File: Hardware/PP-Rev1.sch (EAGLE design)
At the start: 169 parts, among them IC1 LT6004, IC2 TLC6C5912-Q1, Q1 MOSFET-PCHANNEL, Q10 2N7002PW, Q11 2N7002PW, Q12 2N7002PW, Q13 2N7002PW, Q14 2N7002PW, Q15 2N7002PW, Q2 MOSFET-PCHANNEL, Q3 MOSFET-PCHANNEL, Q4 MOSFET-PCHANNEL, Q5 MOSFET-PCHANNEL, Q6 MOSFET-PCHANNEL, Q7 MOSFET-PCHANNEL, Q8 MOSFET-PCHANNEL, Q9 CSD18532, X1 22-23-2031, X2 22-23-2031, X3 22-23-2031, X4 22-23-2031

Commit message: Added launchpad microcontroller library file and into schematic/board. Updated LCD connections to better utilize microcontroller port architecture
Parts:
- added JP4: JST B6B-XH, SparkFun-Connectors:M06POLAR
- added JP5: (no value), SparkFun-Connectors:M16LONGPADS
- added RV1: (no value), SparkFun-Electromechanical:POTTRIM
- added U$13: MSP432P401R-LAUNCHPAD, 2016PowerPackLibraries:MSP432P401R-LAUNCHPAD
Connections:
- removed net N$62: GAUGE_ON.2, IC2./G, R57.2, S2.2
- removed net V_OUT: R38.2, R39.1
- new net CHARGER+: CHARGER+.P$1, JP4.4, Q9.D, Q9.P$1, R43.2, U$10.+, U$11.+
- new net GAUGE_ON: GAUGE_ON.2, IC2./G, R57.2, S2.2, U$13.P6.6
- new net LCD_DB[0]: JP5.7, U$13.P4.0
- new net LCD_DB[1]: JP5.8, U$13.P4.1
- new net LCD_DB[2]: JP5.9, U$13.P4.2
- new net LCD_DB[3]: JP5.10, U$13.P4.3
- new net LCD_DB[4]: JP5.11, U$13.P4.4
- new net LCD_DB[5]: JP5.12, U$13.P4.5
- new net LCD_DB[6]: JP5.13, U$13.P4.6
- new net LCD_DB[7]: JP5.14, U$13.P4.7
- new net LCD_EN: JP5.6, U$13.P3.7
- new net LCD_RS: JP5.4, U$13.P3.5
- new net LCD_RW: JP5.5, U$13.P3.6
- new net LCD_VBACK: JP5.3, RV1.S
- new net N$106: U$13.P6.1
- new net N$107: U$13.P6.2
- new net N$108: U$13.P6.3
- new net N$109: U$13.P6.4
- new net N$110: U$13.P6.5
- new net N$115: JP5.15
- new net N$116: JP5.16
- new net N$45: U$13.P9.4
- new net N$67: U$13.P9.5
- new net N$68: U$13.P9.6
- new net N$93: U$13.P9.7
- new net SUPPLY_CTL: JP4.6, U$13.P2.3
- new net SUPPLY_DC_OK: JP4.1, U$13.P1.7
- new net V_CHECK_OUT: R38.2, R39.1, U$13.P5.4
- net 5V: now also JP5.2, RV1.A, U$13.5V_1, U$13.5V_2, U$13.5V_3, U$13.5V_4
- net BUZZ_1: now also U$13.P5.6
- net BUZZ_2: now also U$13.P5.7
- net CHARGER_CTL: now also U$13.P8.0
- net CHARGER_I_MEAS: now also U$13.P5.2
- net ESTOP_1: now also U$13.P1.5
- net ESTOP_2: now also U$13.P1.6
- net FAN_CTL_1: now also U$13.P2.4
- net FAN_CTL_2: now also U$13.P2.5
- net FAN_CTL_3: now also U$13.P2.6
- net FAN_CTL_4: now also U$13.P2.7
- net FAN_TACH_1: now also U$13.P5.0
- net FAN_TACH_2: now also U$13.P3.3
- net FAN_TACH_3: now also U$13.P3.2
- net FAN_TACH_4: now also U$13.P3.0
- net GND: now also JP4.2, JP4.3, JP4.5, JP5.1, RV1.E, U$13.GND1, U$13.GND2, U$13.GND3, U$13.GND4, U$13.GND5, U$13.GND6, U$13.GND7, U$13.GND8
- net LED_CLR: now also U$13.P10.0
- net LED_RCK: now also U$13.P10.1
- net LED_SER_IN: now also U$13.P10.2
- net LED_SRCK: now also U$13.P10.3
- net N$35: now also U$13.P9.0; no longer CHARGER+.P$1, Q9.D, Q9.P$1, R43.2, U$10.+, U$11.+
- net PACK_GATE: now also U$13.P6.0
- net PACK_I_MEAS: now also U$13.P5.5
- net V_CHECK_ARRAY: now also U$13.P5.3
- net V_CHECK_CHARGER_IN: now also U$13.P5.1
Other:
- note added: "LCD Screen & Power Supply Control"

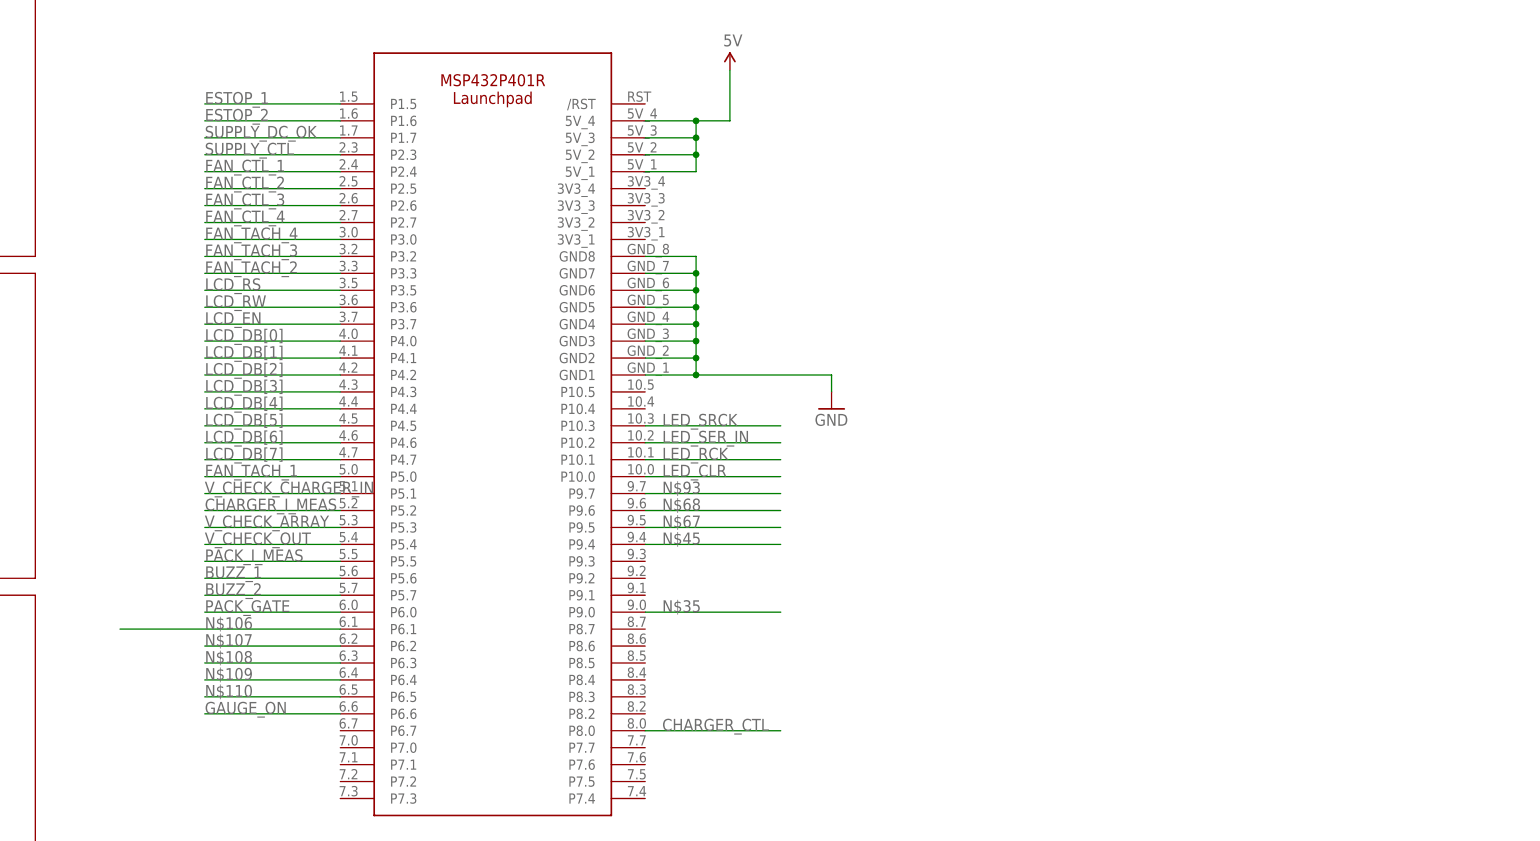
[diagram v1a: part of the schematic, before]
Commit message: Added Wiznet module
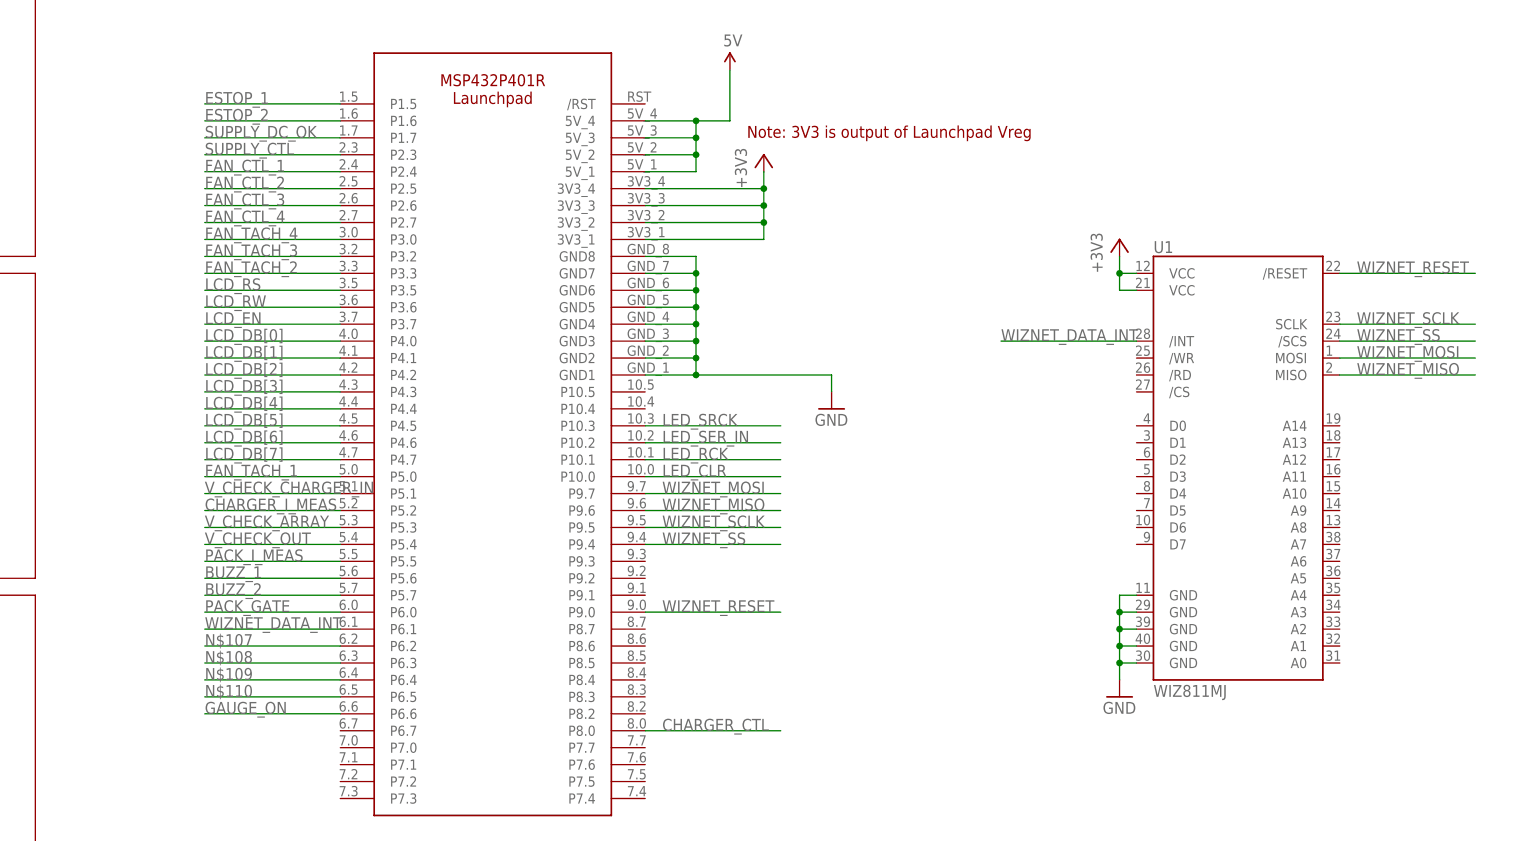
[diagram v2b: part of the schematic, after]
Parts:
- added U1: WIZ811MJ, SparkFun-Boards:WIZ811MJ
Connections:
- removed net N$106: U$13.P6.1
- removed net N$35: U$13.P9.0
- removed net N$45: U$13.P9.4
- removed net N$67: U$13.P9.5
- removed net N$68: U$13.P9.6
- removed net N$93: U$13.P9.7
- new net +3V3: U$13.3V3_1, U$13.3V3_2, U$13.3V3_3, U$13.3V3_4, U1.VCC@1, U1.VCC@2
- new net WIZNET_DATA_INT: U$13.P6.1, U1./INT
- new net WIZNET_MISO: U$13.P9.6, U1.MISO
- new net WIZNET_MOSI: U$13.P9.7, U1.MOSI
- new net WIZNET_RESET: U$13.P9.0, U1./RESET
- new net WIZNET_SCLK: U$13.P9.5, U1.SCLK
- new net WIZNET_SS: U$13.P9.4, U1./SCS
- net GND: now also U1.GND@1, U1.GND@2, U1.GND@3, U1.GND@4, U1.GND@5
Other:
- note added: "Note: 3V3 is output of Launchpad Vreg"
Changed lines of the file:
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@@
 <part name="SUPPLY11" library="SparkFun-Aesthetics" deviceset="5V" device=""/>
 <part name="GND53" library="SparkFun-Aesthetics" deviceset="GND" device=""/>
+<part name="U1" library="SparkFun-Boards" deviceset="WIZ811MJ" device=""/>
+<part name="+3V1" library="supply1" deviceset="+3V3" device=""/>
+<part name="+3V2" library="supply1" deviceset="+3V3" device=""/>
+<part name="GND54" library="SparkFun-Aesthetics" deviceset="GND" device=""/>
 </parts>
 <sheets>
@@
 <wire x1="472.44" y1="193.04" x2="416.56" y2="193.04" width="0.1524" layer="94"/>
 <text x="419.1" y="109.22" size="1.778" layer="94" font="vector">LCD Screen &amp; Power Supply Control</text>
+<text x="355.6" y="317.5" size="1.778" layer="94" font="vector">Note: 3V3 is output of Launchpad Vreg</text>
 </plain>
 <instances>
@@
 <instance part="SUPPLY11" gate="G$1" x="467.36" y="170.18"/>
 <instance part="GND53" gate="1" x="467.36" y="147.32"/>
+<instance part="U1" gate="G$1" x="429.26" y="269.24"/>
+<instance part="+3V1" gate="G$1" x="358.14" y="314.96"/>
+<instance part="+3V2" gate="G$1" x="411.48" y="302.26"/>
+<instance part="GND54" gate="1" x="411.48" y="233.68"/>
 </instances>
 <busses>
@@
 <wire x1="467.36" y1="152.4" x2="467.36" y2="149.86" width="0.1524" layer="91"/>
 </segment>
+<segment>
+<pinref part="U1" gate="G$1" pin="GND@5"/>
+<wire x1="414.02" y1="238.76" x2="411.48" y2="238.76" width="0.1524" layer="91"/>
+<pinref part="GND54" gate="1" pin="GND"/>
+<wire x1="411.48" y1="238.76" x2="411.48" y2="236.22" width="0.1524" layer="91"/>
+<pinref part="U1" gate="G$1" pin="GND@4"/>
+<wire x1="414.02" y1="241.3" x2="411.48" y2="241.3" width="0.1524" layer="91"/>
+<wire x1="411.48" y1="241.3" x2="411.48" y2="238.76" width="0.1524" layer="91"/>
+<junction x="411.48" y="238.76"/>
+<pinref part="U1" gate="G$1" pin="GND@3"/>
+<wire x1="414.02" y1="243.84" x2="411.48" y2="243.84" width="0.1524" layer="91"/>
+<wire x1="411.48" y1="243.84" x2="411.48" y2="241.3" width="0.1524" layer="91"/>
+<junction x="411.48" y="241.3"/>
+<pinref part="U1" gate="G$1" pin="GND@2"/>
+<wire x1="414.02" y1="246.38" x2="411.48" y2="246.38" width="0.1524" layer="91"/>
+<wire x1="411.48" y1="246.38" x2="411.48" y2="243.84" width="0.1524" layer="91"/>
+<junction x="411.48" y="243.84"/>
+<pinref part="U1" gate="G$1" pin="GND@1"/>
+<wire x1="414.02" y1="248.92" x2="411.48" y2="248.92" width="0.1524" layer="91"/>
+<wire x1="411.48" y1="248.92" x2="411.48" y2="246.38" width="0.1524" layer="91"/>
+<junction x="411.48" y="246.38"/>
+</segment>
 </net>
 <net name="N$2" class="0">
@@
 </segment>
 </net>
-<net name="N$106" class="0">
+<net name="WIZNET_DATA_INT" class="0">
 <segment>
 <pinref part="U$13" gate="G$1" pin="P6.1"/>
-<wire x1="294.64" y1="243.84" x2="261.62" y2="243.84" width="0.1524" layer="91"/>
+<wire x1="294.64" y1="243.84" x2="274.32" y2="243.84" width="0.1524" layer="91"/>
 <label x="274.32" y="243.84" size="1.778" layer="95"/>
 </segment>
+<segment>
+<pinref part="U1" gate="G$1" pin="/INT"/>
+<wire x1="414.02" y1="287.02" x2="393.7" y2="287.02" width="0.1524" layer="91"/>
+<label x="393.7" y="287.02" size="1.778" layer="95" font="vector"/>
+</segment>
 </net>
 <net name="N$107" class="0">
@@
 </segment>
 </net>
-<net name="N$35" class="0">
+<net name="WIZNET_RESET" class="0">
 <segment>
 <pinref part="U$13" gate="G$1" pin="P9.0"/>
@@
 <label x="342.9" y="246.38" size="1.778" layer="95"/>
 </segment>
+<segment>
+<pinref part="U1" gate="G$1" pin="/RESET"/>
+<wire x1="444.5" y1="297.18" x2="464.82" y2="297.18" width="0.1524" layer="91"/>
+<label x="447.04" y="297.18" size="1.778" layer="95" font="vector"/>
+</segment>
 </net>
-<net name="N$45" class="0">
+<net name="WIZNET_SS" class="0">
 <segment>
 <pinref part="U$13" gate="G$1" pin="P9.4"/>
@@
 <label x="342.9" y="256.54" size="1.778" layer="95"/>
 </segment>
+<segment>
+<pinref part="U1" gate="G$1" pin="/SCS"/>
+<wire x1="444.5" y1="287.02" x2="464.82" y2="287.02" width="0.1524" layer="91"/>
+<label x="447.04" y="287.02" size="1.778" layer="95" font="vector"/>
+</segment>
 </net>
-<net name="N$67" class="0">
+<net name="WIZNET_SCLK" class="0">
 <segment>
 <pinref part="U$13" gate="G$1" pin="P9.5"/>
@@
 <label x="342.9" y="259.08" size="1.778" layer="95"/>
 </segment>
+<segment>
+<pinref part="U1" gate="G$1" pin="SCLK"/>
+<wire x1="444.5" y1="289.56" x2="464.82" y2="289.56" width="0.1524" layer="91"/>
+<label x="447.04" y="289.56" size="1.778" layer="95" font="vector"/>
+</segment>
 </net>
-<net name="N$68" class="0">
+<net name="WIZNET_MISO" class="0">
 <segment>
 <pinref part="U$13" gate="G$1" pin="P9.6"/>
@@
 <label x="342.9" y="261.62" size="1.778" layer="95"/>
 </segment>
+<segment>
+<pinref part="U1" gate="G$1" pin="MISO"/>
+<wire x1="444.5" y1="281.94" x2="464.82" y2="281.94" width="0.1524" layer="91"/>
+<label x="447.04" y="281.94" size="1.778" layer="95" font="vector"/>
+</segment>
 </net>
-<net name="N$93" class="0">
+<net name="WIZNET_MOSI" class="0">
 <segment>
 <pinref part="U$13" gate="G$1" pin="P9.7"/>
@@
 <label x="342.9" y="264.16" size="1.778" layer="95"/>
 </segment>
+<segment>
+<pinref part="U1" gate="G$1" pin="MOSI"/>
+<wire x1="444.5" y1="284.48" x2="464.82" y2="284.48" width="0.1524" layer="91"/>
+<label x="447.04" y="284.48" size="1.778" layer="95" font="vector"/>
+</segment>
 </net>
 <net name="LCD_VBACK" class="0">
@@
 </segment>
 </net>
+<net name="+3V3" class="0">
+<segment>
+<pinref part="U$13" gate="G$1" pin="3V3_4"/>
+<wire x1="340.36" y1="309.88" x2="358.14" y2="309.88" width="0.1524" layer="91"/>
+<pinref part="+3V1" gate="G$1" pin="+3V3"/>
+<wire x1="358.14" y1="309.88" x2="358.14" y2="312.42" width="0.1524" layer="91"/>
+<pinref part="U$13" gate="G$1" pin="3V3_3"/>
+<wire x1="340.36" y1="307.34" x2="358.14" y2="307.34" width="0.1524" layer="91"/>
+<wire x1="358.14" y1="307.34" x2="358.14" y2="309.88" width="0.1524" layer="91"/>
+<junction x="358.14" y="309.88"/>
+<pinref part="U$13" gate="G$1" pin="3V3_2"/>
+<wire x1="340.36" y1="304.8" x2="358.14" y2="304.8" width="0.1524" layer="91"/>
+<wire x1="358.14" y1="304.8" x2="358.14" y2="307.34" width="0.1524" layer="91"/>
+<junction x="358.14" y="307.34"/>
+<pinref part="U$13" gate="G$1" pin="3V3_1"/>
+<wire x1="340.36" y1="302.26" x2="358.14" y2="302.26" width="0.1524" layer="91"/>
+<wire x1="358.14" y1="302.26" x2="358.14" y2="304.8" width="0.1524" layer="91"/>
+<junction x="358.14" y="304.8"/>
+</segment>
+<segment>
+<pinref part="U1" gate="G$1" pin="VCC@2"/>
+<pinref part="+3V2" gate="G$1" pin="+3V3"/>
+<wire x1="414.02" y1="294.64" x2="411.48" y2="294.64" width="0.1524" layer="91"/>
+<wire x1="411.48" y1="294.64" x2="411.48" y2="297.18" width="0.1524" layer="91"/>
+<pinref part="U1" gate="G$1" pin="VCC@1"/>
+<wire x1="411.48" y1="297.18" x2="411.48" y2="299.72" width="0.1524" layer="91"/>
+<wire x1="414.02" y1="297.18" x2="411.48" y2="297.18" width="0.1524" layer="91"/>
+<junction x="411.48" y="297.18"/>
+</segment>
+</net>

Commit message: Added communication between BMS front-end and microcontroller. Schematic functionally complete.
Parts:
- added R68: 1k, rcl:R-US_R1206
- added R69, R70, R71: 1M, rcl:R-US_R1206
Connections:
- removed net N$107: U$13.P6.2
- removed net N$108: U$13.P6.3
- removed net N$109: U$13.P6.4
- removed net N$110: U$13.P6.5
- new net BMS_CSBI: R69.2, U$1.CSBI, U$13.P6.2
- new net BMS_MISO: R68.1, U$1.SDO, U$13.P6.5
- new net BMS_MOSI: R70.2, U$1.SDI, U$13.P6.4
- new net BMS_SCLK: R71.2, U$1.SCKI, U$13.P6.3
- net +3V3: now also R68.2
- net BMS_VREG: now also R69.1, R70.1, R71.1
- net GND: now also U$1.GPIO1, U$1.GPIO2
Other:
- moved on the sheet: C1, C13, CELL-IN-1, CELL-IN-2, CELL-IN-3, CELL-IN-4, CELL-IN-5, CELL-IN-6, CELL-IN-7, CELL-IN-8, CELL-IN-9, CELL-MEAS-1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
